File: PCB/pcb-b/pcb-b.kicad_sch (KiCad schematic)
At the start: 24 parts, among them J1 Conn_02x05_Counter_Clockwise, J2 Conn_02x05_Counter_Clockwise, K1 HK19F-DCxxV-SHC, Q13 TPCA8120,L1Q, Q3 BC817, Q9 BC817

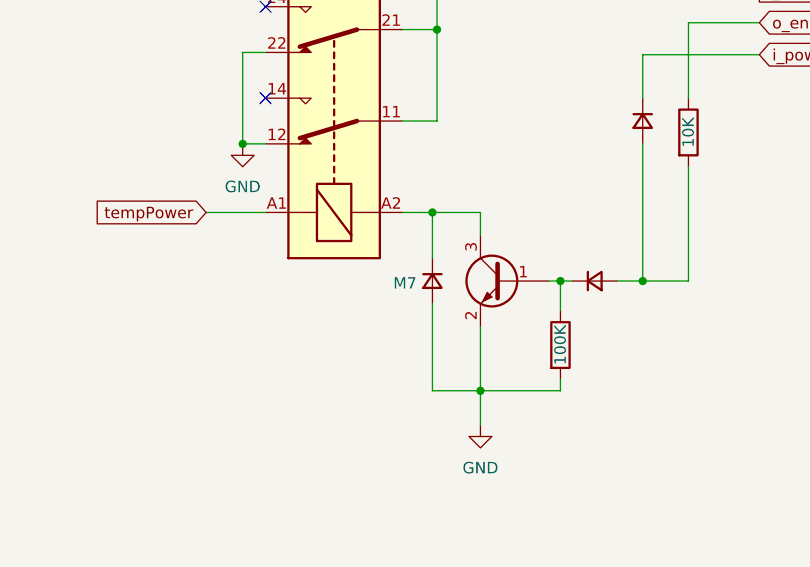
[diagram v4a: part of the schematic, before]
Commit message: Wrong PMEG40T30ER diode's footprint fixed
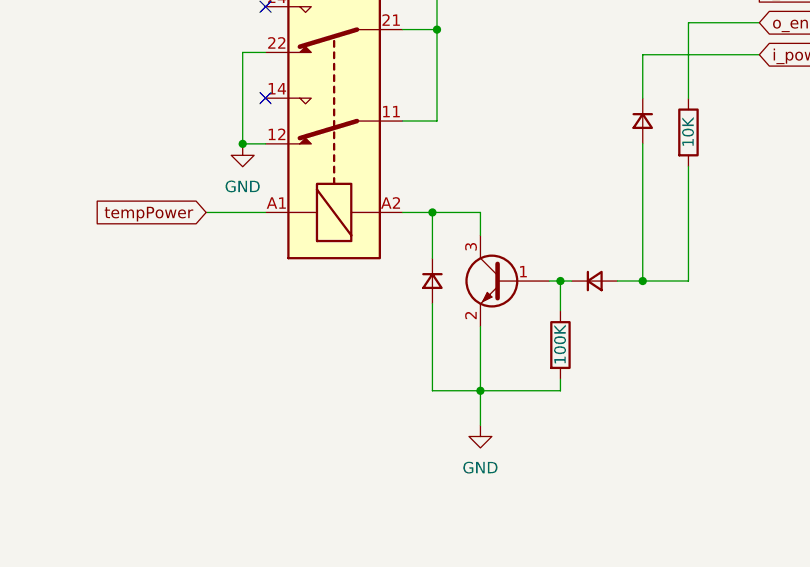
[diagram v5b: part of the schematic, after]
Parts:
- D1, D2, D3: value D_Small -> PMEG40T30ER; footprint Diode_SMD:D_1210_3225Metric_Pad1.42x2.65mm_HandSolder -> Diode_SMD:Nexperia_CFP3_SOD-123W
- flyback-1: value M7 -> PMEG40T30ER; footprint Diode_SMD:D_2114_3652Metric_Pad1.85x3.75mm_HandSolder -> Diode_SMD:Nexperia_CFP3_SOD-123W
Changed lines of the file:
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@@
 			)
 		)
-		(property "Value" "D_Small"
+		(property "Value" "PMEG40T30ER"
 			(at 244.9068 112.776 0)
 			(effects
@@
 			)
 		)
-		(property "Footprint" "Diode_SMD:D_1210_3225Metric_Pad1.42x2.65mm_HandSolder"
+		(property "Footprint" "Diode_SMD:Nexperia_CFP3_SOD-123W"
 			(at 241.554 112.776 90)
 			(effects
@@
 			)
 		)
-		(property "Value" "D_Small"
+		(property "Value" "PMEG40T30ER"
 			(at 71.882 132.0292 0)
 			(effects
@@
 			)
 		)
-		(property "Footprint" "Diode_SMD:D_1210_3225Metric_Pad1.42x2.65mm_HandSolder"
+		(property "Footprint" "Diode_SMD:Nexperia_CFP3_SOD-123W"
 			(at 71.882 135.382 90)
 			(effects
@@
 			)
 		)
-		(property "Value" "M7"
+		(property "Value" "PMEG40T30ER"
 			(at 215.138 130.81 90)
 			(effects
@@
 					(size 1.27 1.27)
 				)
-			)
-		)
-		(property "Footprint" "Diode_SMD:D_2114_3652Metric_Pad1.85x3.75mm_HandSolder"
+				(hide yes)
+			)
+		)
+		(property "Footprint" "Diode_SMD:Nexperia_CFP3_SOD-123W"
 			(at 218.186 130.556 90)
 			(effects
@@
 			)
 		)
-		(property "Value" "D_Small"
+		(property "Value" "PMEG40T30ER"
 			(at 236.22 127.2032 0)
 			(effects
@@
 			)
 		)
-		(property "Footprint" "Diode_SMD:D_1210_3225Metric_Pad1.42x2.65mm_HandSolder"
+		(property "Footprint" "Diode_SMD:Nexperia_CFP3_SOD-123W"
 			(at 236.22 130.556 90)
 			(effects
